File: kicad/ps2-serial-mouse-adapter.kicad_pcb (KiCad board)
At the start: 2 copper layers, 60.3 x 31.1 mm, 11 parts, among them U1 Arduino_Mini, U2 MAX232

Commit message: Update gerber files, minor cleanups
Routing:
- net Net-(C2-Pad1): track 48.2 -> 47.4 mm
- net VCC: track 22.3 -> 21.6 mm

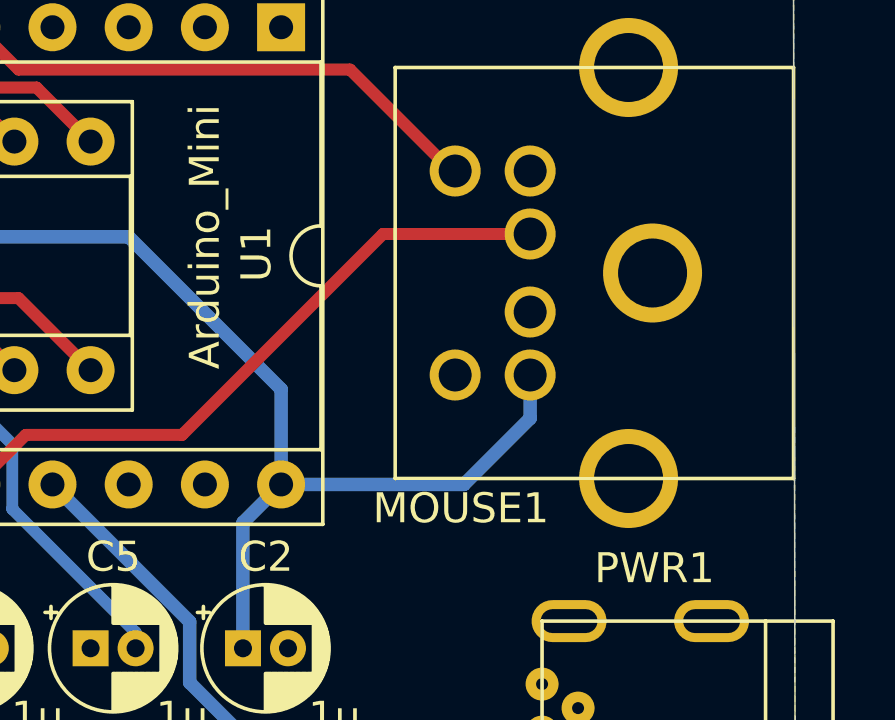
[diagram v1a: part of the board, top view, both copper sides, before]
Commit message: Add necroware kicad library
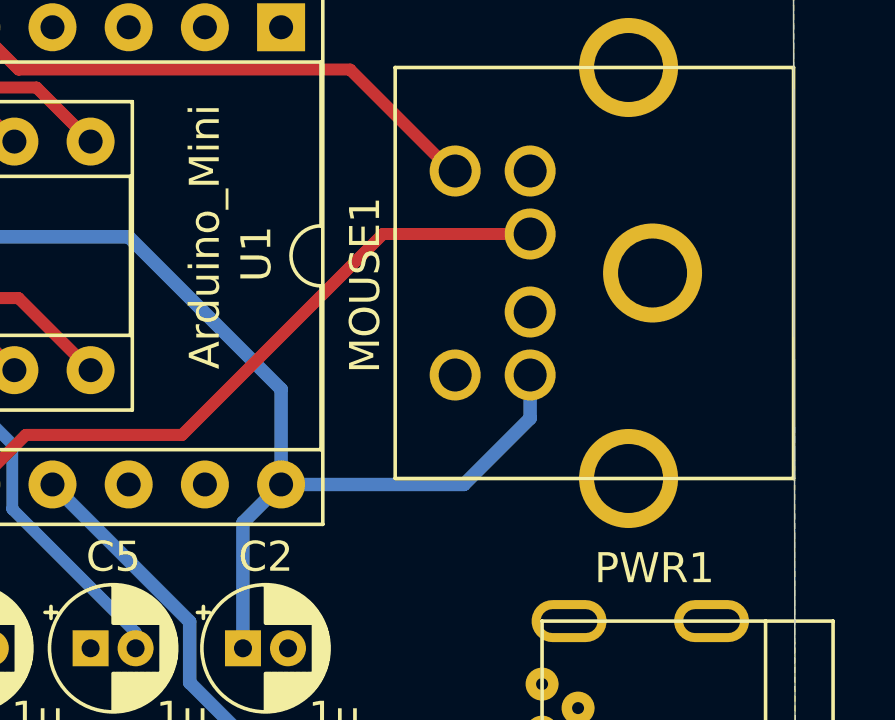
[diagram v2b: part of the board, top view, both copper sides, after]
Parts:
- MOUSE1: footprint MyLibrary:Mini_DIN_6_LCSC_C77848 -> Necroware:Mini_DIN_6_LCSC_C77848
